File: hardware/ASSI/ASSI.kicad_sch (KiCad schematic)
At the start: 39 parts

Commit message: Add resistor and capacitor values to ASSI board
- Red: 2 x 300 ohm, green: 1 x 1k, blue: 3 x 43 ohm per LED row
- C3, C4: 100 nF
- Regenerate schematic PDF, images and fabrication output
- Update README with the component values

Co-Authored-By: Claude Opus 5.5 <noreply@anthropic.com>
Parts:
- C3, C4: value C -> 100nF
- R1, R13, R15, R2, R7, R9: value R -> 300
- R10, R16, R3: value R -> 1k
- R11, R12, R14, R17, R18, R4, R5, R6, R8: value R -> 43
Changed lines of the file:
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@@
 			)
 		)
-		(property "Value" "R"
+		(property "Value" "43"
 			(at 142.24 130.81 90)
-			(hide yes)
 			(show_name no)
 			(do_not_autoplace no)
@@
 			)
 		)
-		(property "Value" "R"
+		(property "Value" "1k"
 			(at 132.08 58.42 90)
-			(hide yes)
 			(show_name no)
 			(do_not_autoplace no)
@@
 			)
 		)
-		(property "Value" "R"
+		(property "Value" "300"
 			(at 132.08 53.34 90)
-			(hide yes)
 			(show_name no)
 			(do_not_autoplace no)
@@
 			)
 		)
-		(property "Value" "R"
+		(property "Value" "43"
 			(at 142.24 97.79 90)
-			(hide yes)
 			(show_name no)
 			(do_not_autoplace no)
@@
 			)
 		)
-		(property "Value" "R"
+		(property "Value" "43"
 			(at 132.08 97.79 90)
-			(hide yes)
 			(show_name no)
 			(do_not_autoplace no)
@@
 			)
 		)
-		(property "Value" "R"
+		(property "Value" "300"
 			(at 132.08 120.65 90)
-			(hide yes)
 			(show_name no)
 			(do_not_autoplace no)
@@
 			)
 		)
-		(property "Value" "R"
+		(property "Value" "300"
 			(at 132.08 87.63 90)
-			(hide yes)
 			(show_name no)
 			(do_not_autoplace no)
@@
 			)
 		)
-		(property "Value" "C"
+		(property "Value" "100nF"
 			(at 64.77 80.0099 0)
 			(show_name no)
@@
 			)
 		)
-		(property "Value" "R"
+		(property "Value" "300"
 			(at 121.92 87.63 90)
-			(hide yes)
 			(show_name no)
 			(do_not_autoplace no)
@@
 			)
 		)
-		(property "Value" "R"
+		(property "Value" "300"
 			(at 121.92 120.65 90)
-			(hide yes)
 			(show_name no)
 			(do_not_autoplace no)
@@
 			)
 		)
-		(property "Value" "R"
+		(property "Value" "43"
 			(at 132.08 130.81 90)
-			(hide yes)
 			(show_name no)
 			(do_not_autoplace no)
@@
 			)
 		)
-		(property "Value" "R"
+		(property "Value" "43"
 			(at 132.08 63.5 90)
-			(hide yes)
 			(show_name no)
 			(do_not_autoplace no)
@@
 			)
 		)
-		(property "Value" "R"
+		(property "Value" "43"
 			(at 121.92 97.79 90)
-			(hide yes)
 			(show_name no)
 			(do_not_autoplace no)
@@
 			)
 		)
-		(property "Value" "R"
+		(property "Value" "1k"
 			(at 132.08 125.73 90)
-			(hide yes)
 			(show_name no)
 			(do_not_autoplace no)
@@
 			)
 		)
-		(property "Value" "R"
+		(property "Value" "1k"
 			(at 132.08 92.71 90)
-			(hide yes)
 			(show_name no)
 			(do_not_autoplace no)
@@
 			)
 		)
-		(property "Value" "R"
+		(property "Value" "300"
 			(at 121.92 53.34 90)
-			(hide yes)
 			(show_name no)
 			(do_not_autoplace no)
@@
 			)
 		)
-		(property "Value" "R"
+		(property "Value" "43"
 			(at 121.92 130.81 90)
-			(hide yes)
 			(show_name no)
 			(do_not_autoplace no)
@@
 			)
 		)
-		(property "Value" "C"
+		(property "Value" "100nF"
 			(at 64.77 49.5299 0)
 			(show_name no)
@@
 			)
 		)
-		(property "Value" "R"
+		(property "Value" "43"
 			(at 121.92 63.5 90)
-			(hide yes)
 			(show_name no)
 			(do_not_autoplace no)
@@
 			)
 		)
-		(property "Value" "R"
+		(property "Value" "43"
 			(at 142.24 63.5 90)
-			(hide yes)
 			(show_name no)
 			(do_not_autoplace no)

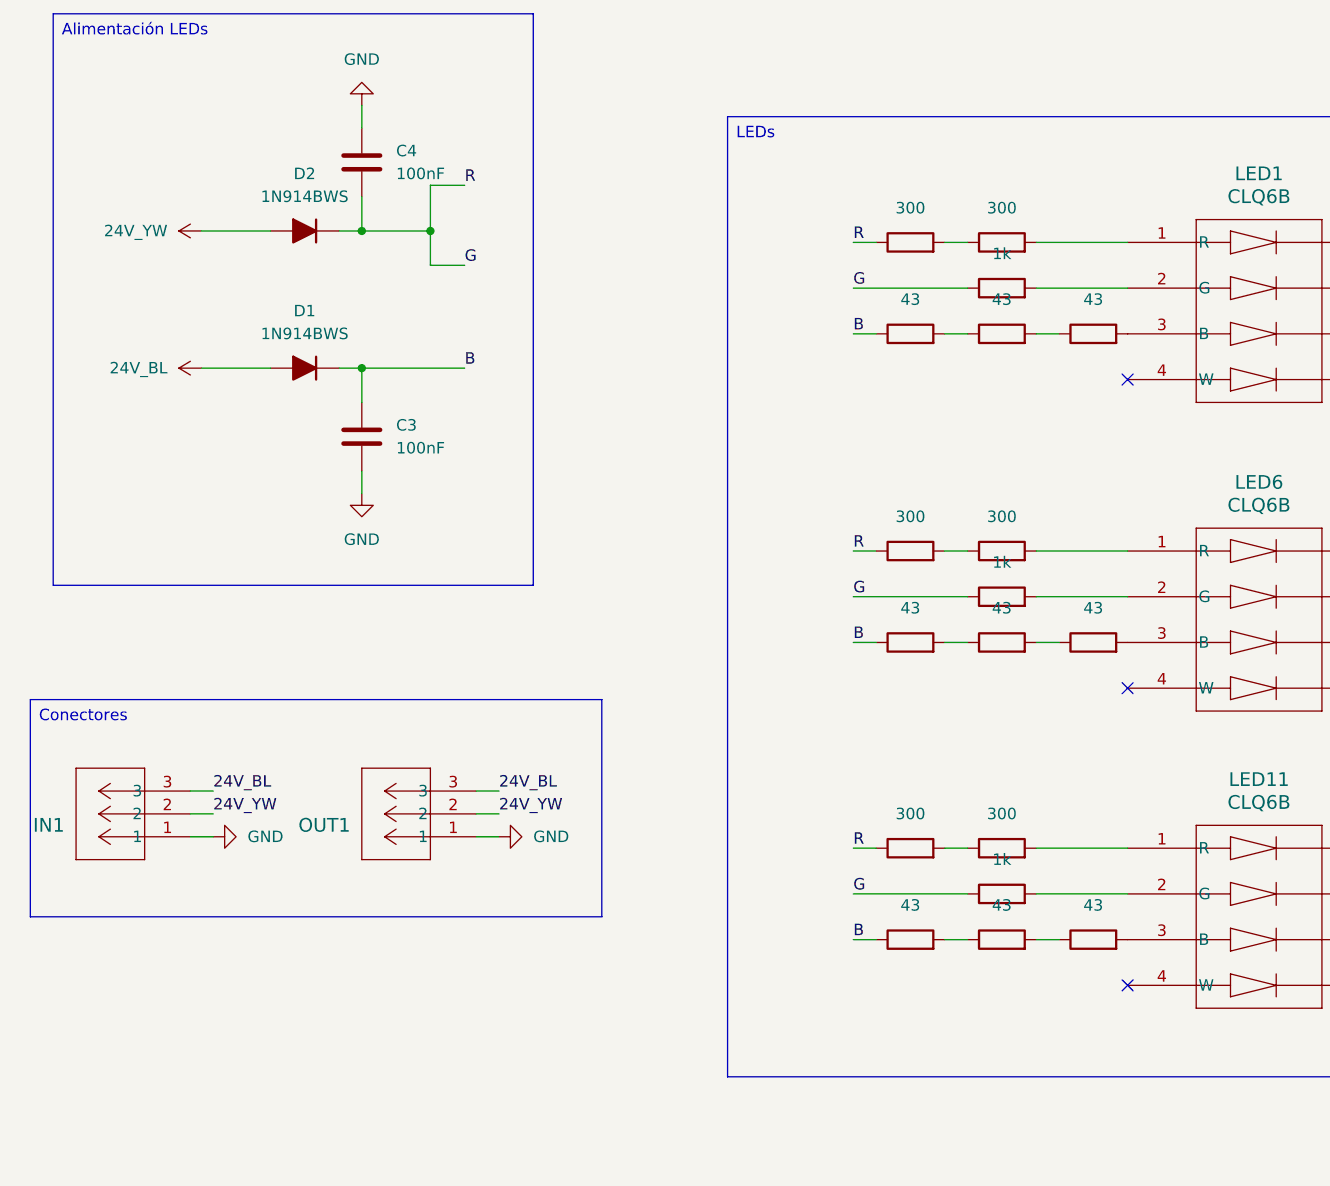
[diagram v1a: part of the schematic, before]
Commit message: Address design review issues on ASSI board
- D1/D2: PMEG4010CEH Schottky (SOD-123F), blue resistors 3 x 47 ohm
- Resistors: Panasonic ERJ-P08 1206 0.66 W, rating in value and MPN,
  derating check against the datasheet in the README
- Footprints from standard KiCad libraries, ISC logo from IFS-KicadLib
- 4 x M3 non-plated mounting holes with 8 mm copper keep-out
- Power net class (0.8 mm) and LED net class (0.5 mm), GND stitching vias
- Manufacturer and MPN fields on every part, bom.csv and positions.csv
- Regenerate schematic PDF, images and fabrication output
- README: rules compliance, mounting configuration, currents and power,
  updated PCB data, BOM with MPNs and open points

Co-Authored-By: Claude Opus 5.5 <noreply@anthropic.com>
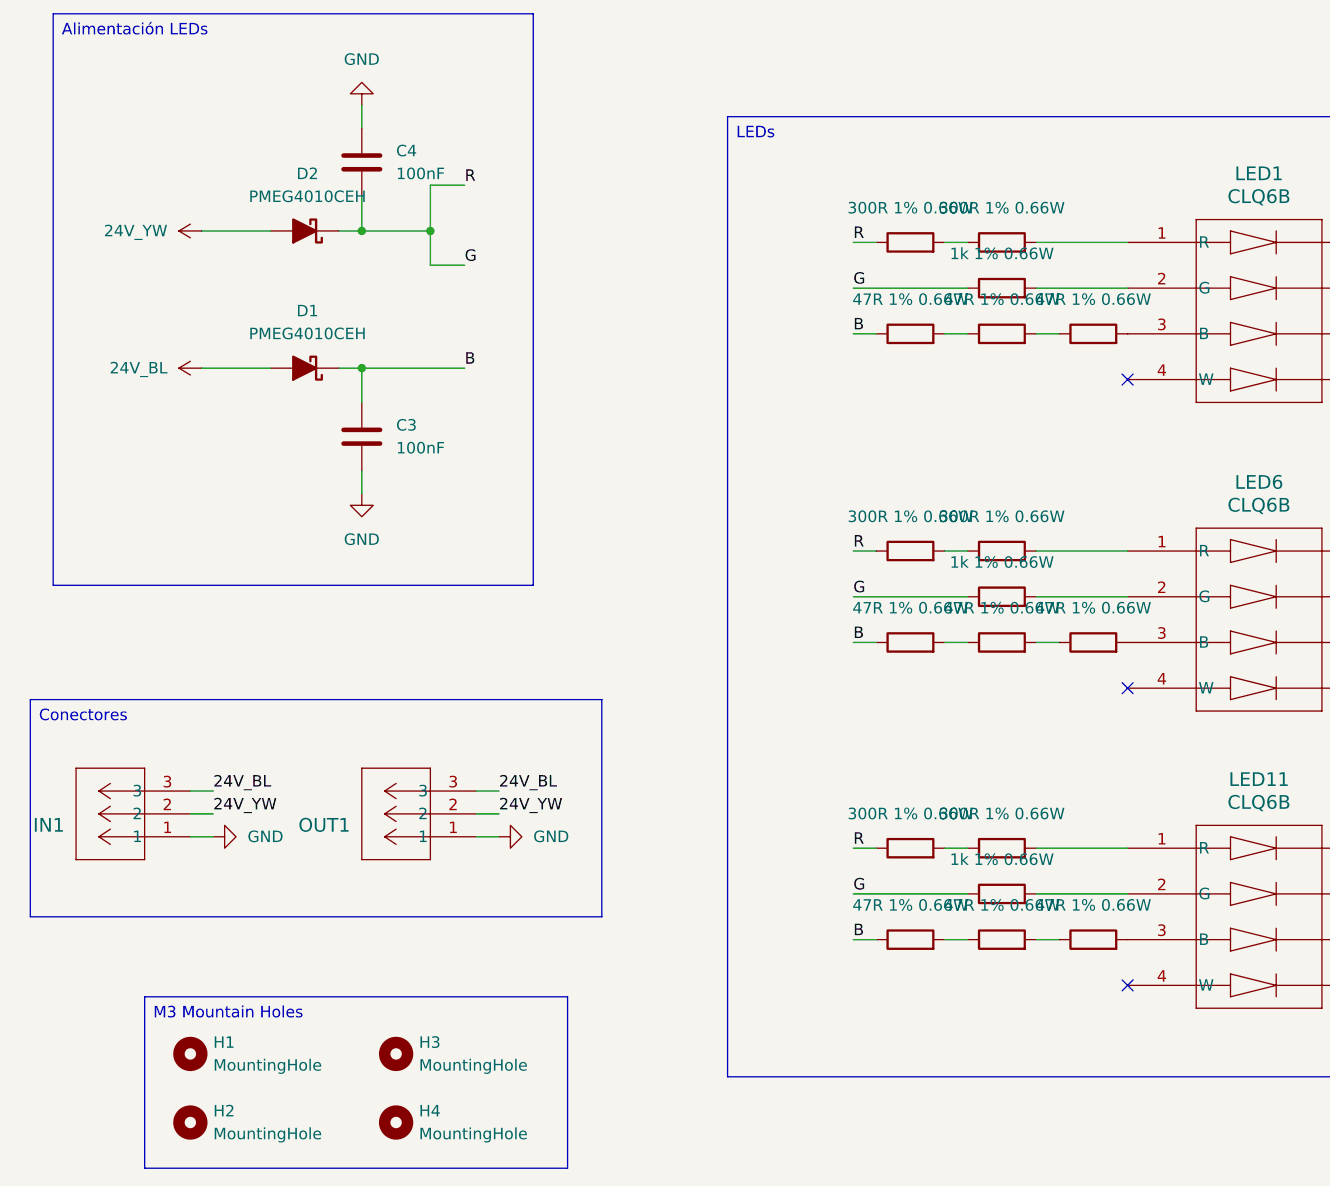
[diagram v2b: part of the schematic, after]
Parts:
- removed D1, D2: 1N914BWS, PCM_Diode_SMD_AKL:D_SOD-323F, symbol PCM_Diode_AKL:1N914BWS
- added D1, D2: PMEG4010CEH, Diode_SMD:D_SOD-123F, symbol PCM_Diode_Schottky_AKL:PMEG4010CEH
- added H1, H2, H3, H4: MountingHole, MountingHole:MountingHole_3.2mm_M3, symbol Mechanical:MountingHole
- C3, C4: MPN (none) -> CL21B104KBCNNNC; Manufacturer (none) -> Samsung Electro-Mechanics
- IN1, OUT1: MPN (none) -> 43650-0300; Manufacturer (none) -> Molex
- LED1, LED10, LED11, LED12, LED13, LED14, LED15, LED2, LED3, LED4, LED5, LED6, LED7, LED8, LED9: MPN (none) -> CLQ6B-TKW-S1L1R1H1TBB7935BB3; Manufacturer (none) -> CreeLED
- R1, R13, R15, R2, R7, R9: value 300 -> 300R 1% 0.66W; footprint PCM_Resistor_SMD_AKL:R_1206_3216Metric_Pad1.30x1.75mm_HandSolder -> Resistor_SMD:R_1206_3216Metric_Pad1.30x1.75mm_HandSolder; MPN (none) -> ERJ-P08F3000V; Manufacturer (none) -> Panasonic
- R10, R16, R3: value 1k -> 1k 1% 0.66W; footprint PCM_Resistor_SMD_AKL:R_1206_3216Metric_Pad1.30x1.75mm_HandSolder -> Resistor_SMD:R_1206_3216Metric_Pad1.30x1.75mm_HandSolder; MPN (none) -> ERJ-P08F1001V; Manufacturer (none) -> Panasonic
- R11, R12, R14, R17, R18, R4, R5, R6, R8: value 43 -> 47R 1% 0.66W; footprint PCM_Resistor_SMD_AKL:R_1206_3216Metric_Pad1.30x1.75mm_HandSolder -> Resistor_SMD:R_1206_3216Metric_Pad1.30x1.75mm_HandSolder; MPN (none) -> ERJ-P08F47R0V; Manufacturer (none) -> Panasonic
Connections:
- net 24V_BL: now also D1.2 (A)
- net 24V_YW: now also D2.2 (A)
- net B: now also D1.1 (K)
- net G: now also D2.1 (K)
